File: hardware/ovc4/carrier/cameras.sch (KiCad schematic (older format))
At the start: 5 parts, among them U1 Jetson_Nano, U12 PICAM_Expandable, U13 PICAM, U14 PICAM_Expandable, U15 PICAM

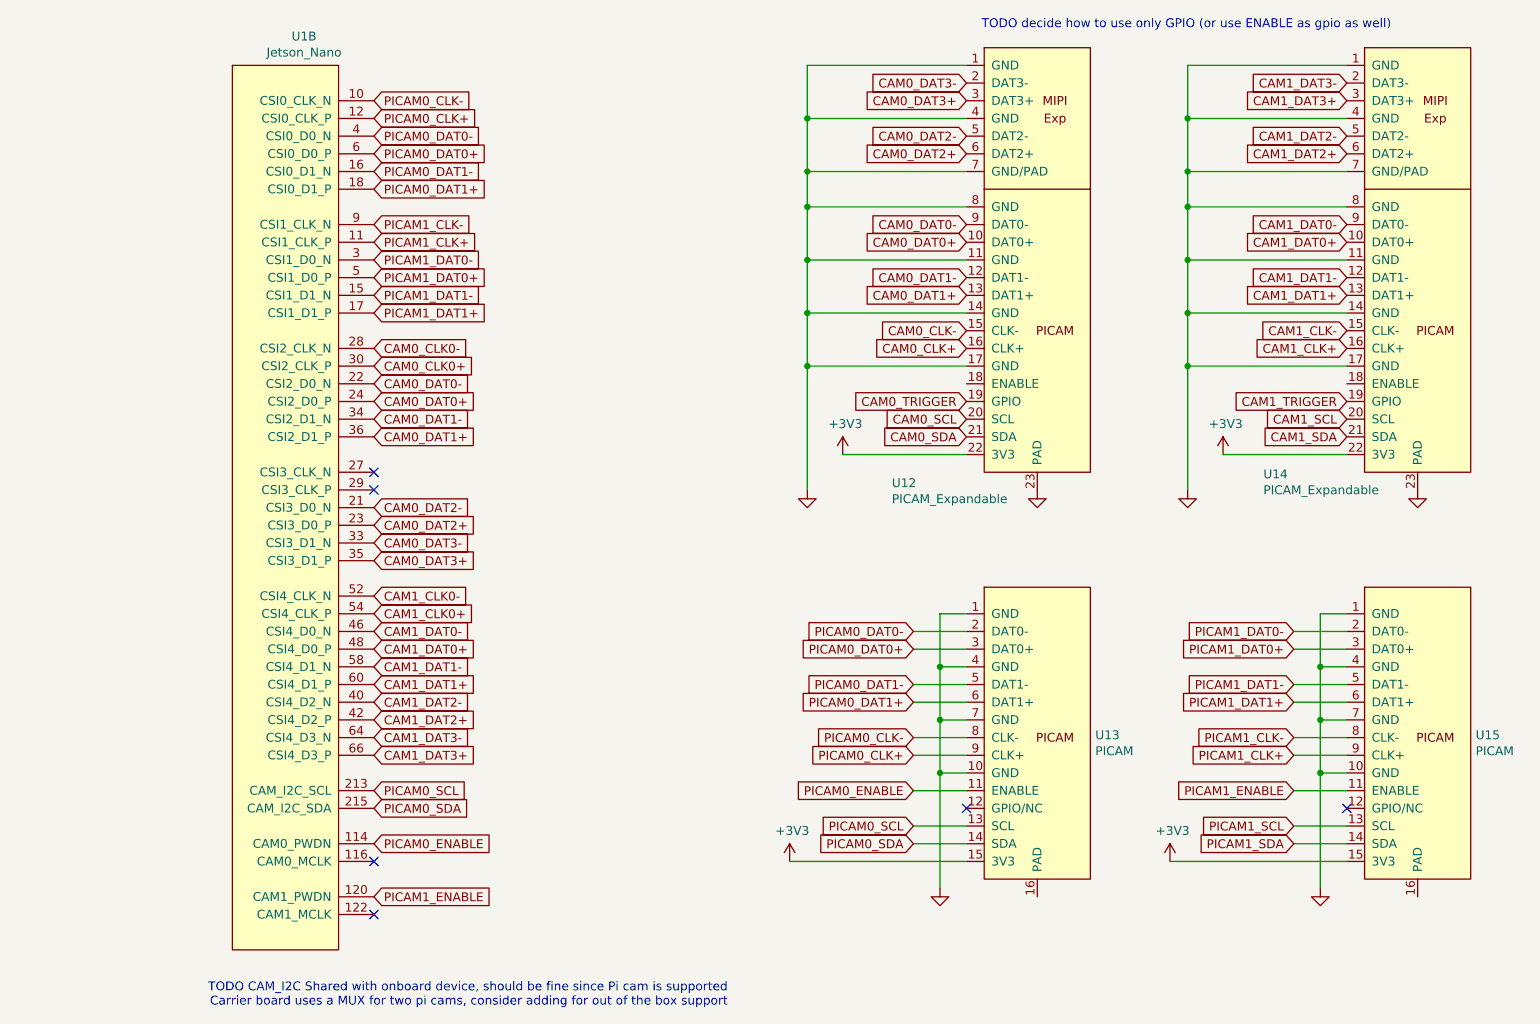
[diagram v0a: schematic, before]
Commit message: Several camera interface + USB fixes
Signed-off-by: Luca Della Vedova <luca@openrobotics.org>
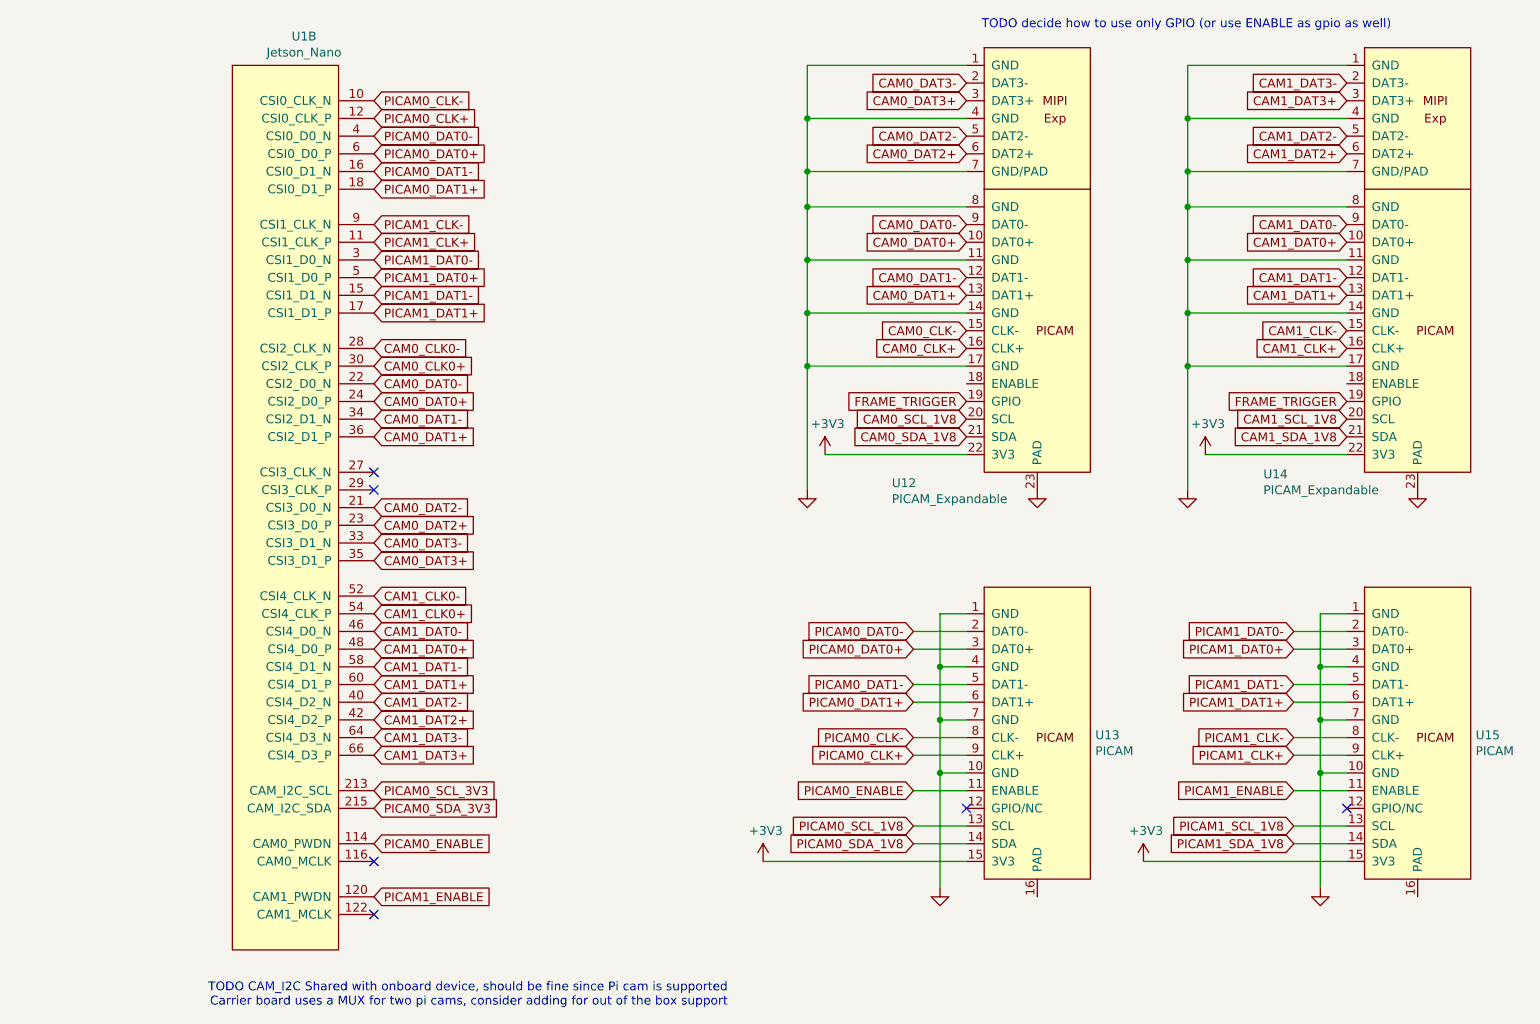
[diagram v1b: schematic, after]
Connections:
- net CAM1_TRIGGER is gone; now on net FRAME_TRIGGER: U14.19 (GPIO)
- net CAM0_SCL renamed CAM0_SCL_1V8
- net CAM0_SDA renamed CAM0_SDA_1V8
- net CAM0_TRIGGER renamed FRAME_TRIGGER
- net CAM1_SCL renamed CAM1_SCL_1V8
- net CAM1_SDA renamed CAM1_SDA_1V8
- net PICAM0_SCL renamed PICAM0_SCL_1V8
- net PICAM0_SCL_1V8: no longer U1.213 (CAM_I2C_SCL)
- net PICAM0_SDA renamed PICAM0_SDA_1V8
- net PICAM0_SDA_1V8: no longer U1.215 (CAM_I2C_SDA)
- net PICAM1_SCL renamed PICAM1_SCL_1V8
- net PICAM1_SDA renamed PICAM1_SDA_1V8
- new net PICAM0_SCL_3V3: U1.213 (CAM_I2C_SCL)
- new net PICAM0_SDA_3V3: U1.215 (CAM_I2C_SDA)
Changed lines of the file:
@@
 NoConn ~ 2150 6000
 Wire Wire Line
-	4500 5700 5500 5700
+	4350 5700 5500 5700
 Wire Wire Line
 	4600 1200 4600 1500
@@
 	4600 2900 5500 2900
 Wire Wire Line
-	4800 3400 5500 3400
+	4700 3400 5500 3400
 Wire Wire Line
 	5200 4400 5500 4400
@@
 	5500 4300 5350 4300
 Wire Wire Line
-	6650 5700 7650 5700
+	6500 5700 7650 5700
 Wire Wire Line
 	6750 1200 6750 1500
@@
 	6750 2900 7650 2900
 Wire Wire Line
-	6950 3400 7650 3400
+	6850 3400 7650 3400
 Wire Wire Line
 	7350 4400 7650 4400
@@
 CAM1_DAT3+
 Text GLabel 2150 5300 2    50   Input ~ 0
-PICAM0_SCL
+PICAM0_SCL_3V3
 Text GLabel 2150 5400 2    50   Input ~ 0
-PICAM0_SDA
+PICAM0_SDA_3V3
 Text GLabel 2150 5600 2    50   Input ~ 0
 PICAM0_ENABLE
@@
 PICAM0_ENABLE
 Text GLabel 5200 5500 0    50   Input ~ 0
-PICAM0_SCL
+PICAM0_SCL_1V8
 Text GLabel 5200 5600 0    50   Input ~ 0
-PICAM0_SDA
+PICAM0_SDA_1V8
 Text GLabel 5500 1300 0    50   Input ~ 0
 CAM0_DAT3-
@@
 CAM0_CLK+
 Text GLabel 5500 3100 0    50   Input ~ 0
-CAM0_TRIGGER
+FRAME_TRIGGER
 Text GLabel 5500 3200 0    50   Input ~ 0
-CAM0_SCL
+CAM0_SCL_1V8
 Text GLabel 5500 3300 0    50   Input ~ 0
-CAM0_SDA
+CAM0_SDA_1V8
 Text GLabel 7350 4400 0    50   Input ~ 0
 PICAM1_DAT0-
@@
 PICAM1_ENABLE
 Text GLabel 7350 5500 0    50   Input ~ 0
-PICAM1_SCL
+PICAM1_SCL_1V8
 Text GLabel 7350 5600 0    50   Input ~ 0
-PICAM1_SDA
+PICAM1_SDA_1V8
 Text GLabel 7650 1300 0    50   Input ~ 0
 CAM1_DAT3-
@@
 CAM1_CLK+
 Text GLabel 7650 3100 0    50   Input ~ 0
-CAM1_TRIGGER
+FRAME_TRIGGER
 Text GLabel 7650 3200 0    50   Input ~ 0
-CAM1_SCL
+CAM1_SCL_1V8
 Text GLabel 7650 3300 0    50   Input ~ 0
-CAM1_SDA
+CAM1_SDA_1V8
 $Comp
 L power:+3V3 #PWR0170
 U 1 1 5EAFC299
-P 4500 5700
-F 0 "#PWR0170" H 4500 5550 50  0001 C CNN
-F 1 "+3V3" H 4515 5873 50  0000 C CNN
-F 2 "" H 4500 5700 50  0001 C CNN
-F 3 "" H 4500 5700 50  0001 C CNN
-	1    4500 5700
+P 4350 5700
+F 0 "#PWR0170" H 4350 5550 50  0001 C CNN
+F 1 "+3V3" H 4365 5873 50  0000 C CNN
+F 2 "" H 4350 5700 50  0001 C CNN
+F 3 "" H 4350 5700 50  0001 C CNN
+	1    4350 5700
 	1    0    0    -1
 $EndComp
@@
 L power:+3V3 #PWR0167
 U 1 1 5EB5706A
-P 4800 3400
-F 0 "#PWR0167" H 4800 3250 50  0001 C CNN
-F 1 "+3V3" H 4815 3573 50  0000 C CNN
-F 2 "" H 4800 3400 50  0001 C CNN
-F 3 "" H 4800 3400 50  0001 C CNN
-	1    4800 3400
+P 4700 3400
+F 0 "#PWR0167" H 4700 3250 50  0001 C CNN
+F 1 "+3V3" H 4715 3573 50  0000 C CNN
+F 2 "" H 4700 3400 50  0001 C CNN
+F 3 "" H 4700 3400 50  0001 C CNN
+	1    4700 3400
 	1    0    0    -1
 $EndComp
@@
 L power:+3V3 #PWR0173
 U 1 1 5EB00BB6
-P 6650 5700
-F 0 "#PWR0173" H 6650 5550 50  0001 C CNN
-F 1 "+3V3" H 6665 5873 50  0000 C CNN
-F 2 "" H 6650 5700 50  0001 C CNN
-F 3 "" H 6650 5700 50  0001 C CNN
-	1    6650 5700
+P 6500 5700
+F 0 "#PWR0173" H 6500 5550 50  0001 C CNN
+F 1 "+3V3" H 6515 5873 50  0000 C CNN
+F 2 "" H 6500 5700 50  0001 C CNN
+F 3 "" H 6500 5700 50  0001 C CNN
+	1    6500 5700
 	1    0    0    -1
 $EndComp
@@
 L power:+3V3 #PWR0171
 U 1 1 5EB27C8C
-P 6950 3400
-F 0 "#PWR0171" H 6950 3250 50  0001 C CNN
-F 1 "+3V3" H 6965 3573 50  0000 C CNN
-F 2 "" H 6950 3400 50  0001 C CNN
-F 3 "" H 6950 3400 50  0001 C CNN
-	1    6950 3400
+P 6850 3400
+F 0 "#PWR0171" H 6850 3250 50  0001 C CNN
+F 1 "+3V3" H 6865 3573 50  0000 C CNN
+F 2 "" H 6850 3400 50  0001 C CNN
+F 3 "" H 6850 3400 50  0001 C CNN
+	1    6850 3400
 	1    0    0    -1
 $EndComp
